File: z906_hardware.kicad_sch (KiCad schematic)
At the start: 22 parts, among them J1 USB_C_Receptacle_USB2.0_14P, J3 DE_15 Amplifier, J4 DE15 Console, U1 ESP32-S3-WROOM-1, U2 AP63203WU, U3 PCM5102A, U4 TPD2EUSB30, U5 TPD1E05U06DYA, U6 TPS7A4533

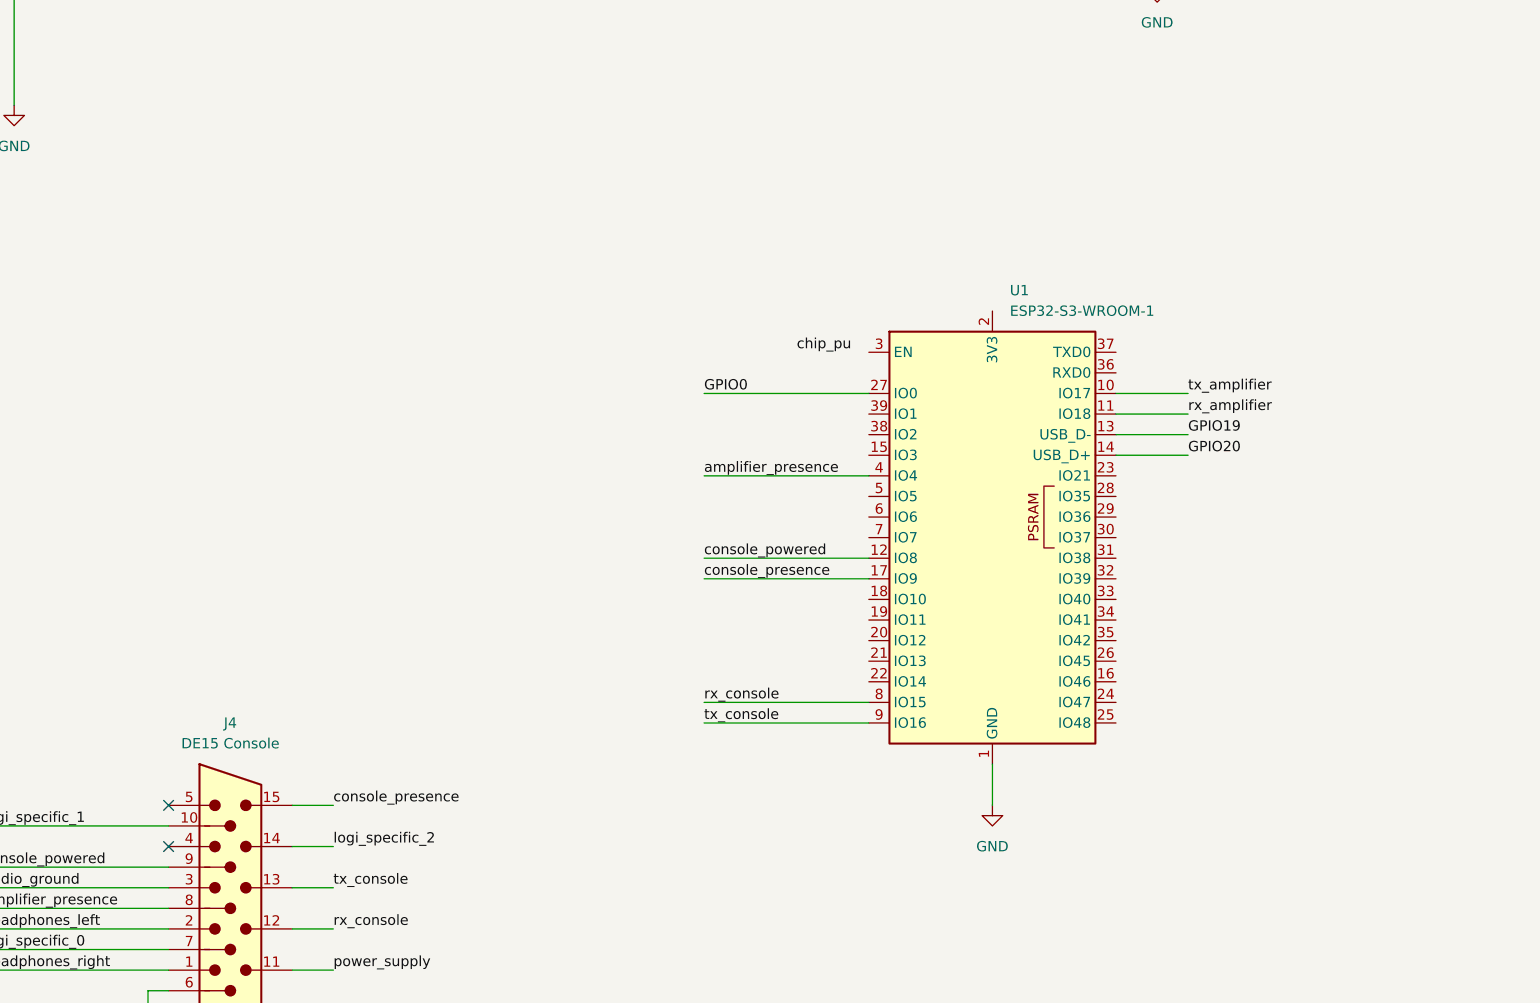
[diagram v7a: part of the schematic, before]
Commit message: add pcm1860
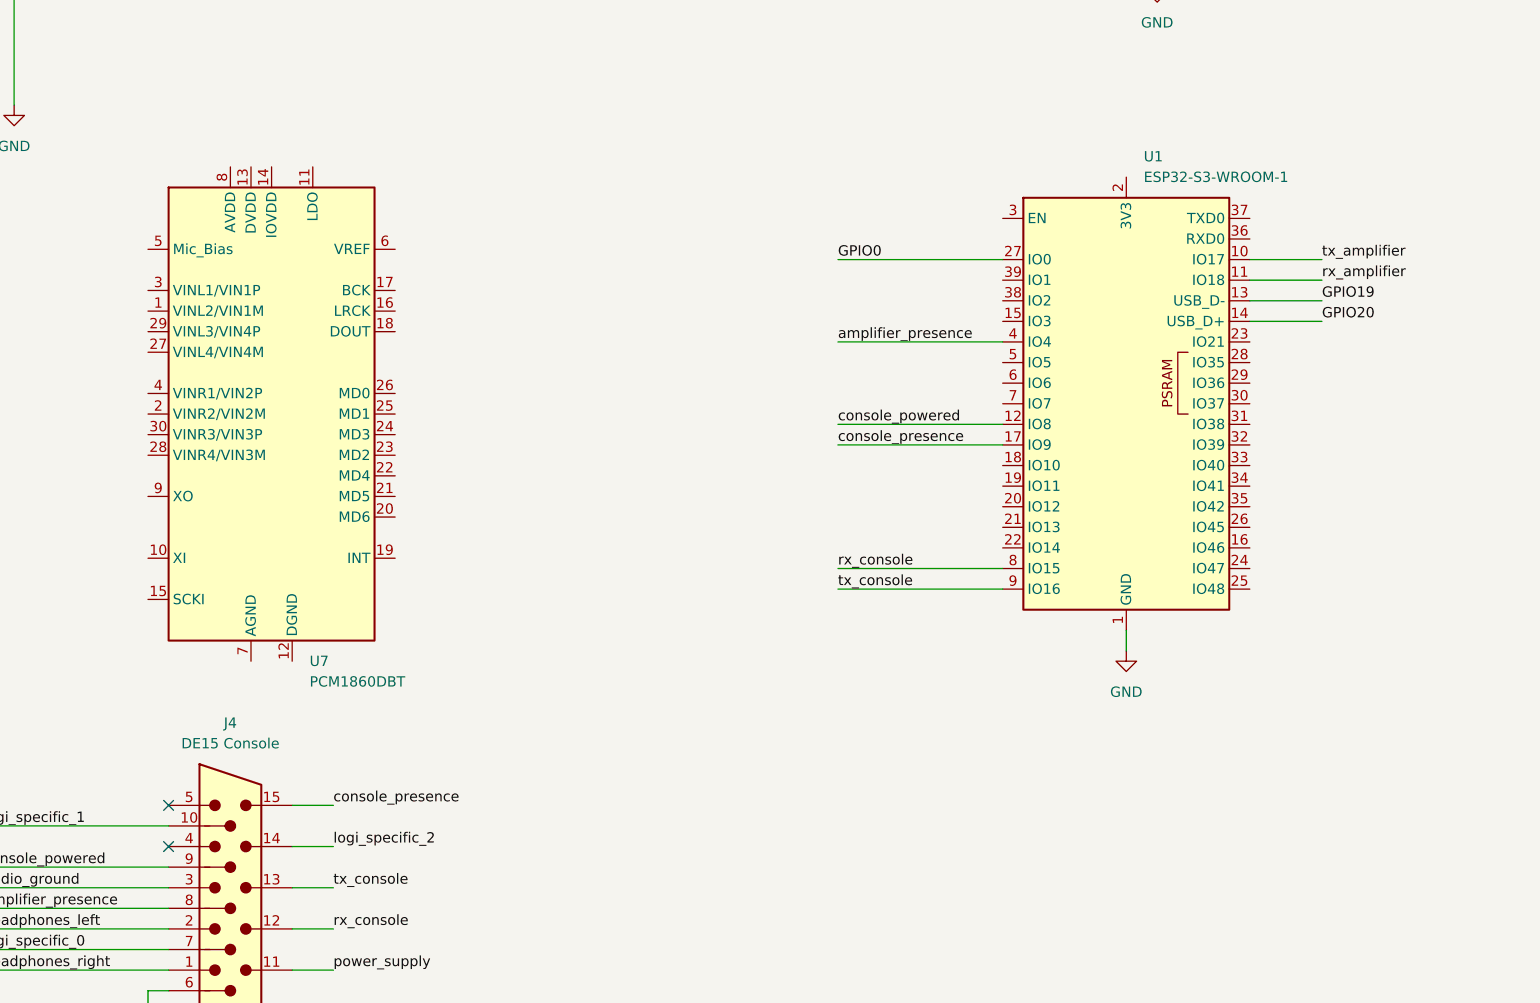
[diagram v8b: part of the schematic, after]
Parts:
- added U7: PCM1860DBT, Package_SO:TSSOP-30_4.4x7.8mm_P0.5mm, symbol Audio:PCM1860DBT
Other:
- moved on the sheet: U1
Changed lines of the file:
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@@
 	(wire
 		(pts
-			(xy 182.88 146.05) (xy 203.2 146.05)
+			(xy 199.39 129.54) (xy 219.71 129.54)
 		)
 		(stroke
@@
 	(wire
 		(pts
-			(xy 182.88 115.57) (xy 203.2 115.57)
+			(xy 199.39 99.06) (xy 219.71 99.06)
 		)
 		(stroke
@@
 	(wire
 		(pts
-			(xy 233.68 107.95) (xy 242.57 107.95)
+			(xy 250.19 91.44) (xy 259.08 91.44)
 		)
 		(stroke
@@
 	(wire
 		(pts
-			(xy 182.88 128.27) (xy 203.2 128.27)
+			(xy 199.39 111.76) (xy 219.71 111.76)
 		)
 		(stroke
@@
 	(wire
 		(pts
-			(xy 182.88 105.41) (xy 203.2 105.41)
+			(xy 199.39 88.9) (xy 219.71 88.9)
 		)
 		(stroke
@@
 	(wire
 		(pts
-			(xy 218.44 151.13) (xy 218.44 156.21)
+			(xy 234.95 134.62) (xy 234.95 137.16)
 		)
 		(stroke
@@
 	(wire
 		(pts
-			(xy 233.68 113.03) (xy 242.57 113.03)
+			(xy 250.19 96.52) (xy 259.08 96.52)
 		)
 		(stroke
@@
 	(wire
 		(pts
-			(xy 233.68 110.49) (xy 242.57 110.49)
+			(xy 250.19 93.98) (xy 259.08 93.98)
 		)
 		(stroke
@@
 	(wire
 		(pts
-			(xy 182.88 125.73) (xy 203.2 125.73)
+			(xy 199.39 109.22) (xy 219.71 109.22)
 		)
 		(stroke
@@
 	(wire
 		(pts
-			(xy 233.68 105.41) (xy 242.57 105.41)
+			(xy 250.19 88.9) (xy 259.08 88.9)
 		)
 		(stroke
@@
 	(wire
 		(pts
-			(xy 182.88 143.51) (xy 203.2 143.51)
+			(xy 199.39 127) (xy 219.71 127)
 		)
 		(stroke
@@
 	)
 	(label "rx_amplifier"
-		(at 242.57 107.95 0)
+		(at 259.08 91.44 0)
 		(effects
 			(font
@@
 	)
 	(label "tx_console"
-		(at 182.88 146.05 0)
+		(at 199.39 129.54 0)
 		(effects
 			(font
@@
 	)
 	(label "GPIO0"
-		(at 182.88 105.41 0)
+		(at 199.39 88.9 0)
 		(effects
 			(font
@@
 	)
 	(label "GPIO19"
-		(at 242.57 110.49 0)
+		(at 259.08 93.98 0)
 		(effects
 			(font
@@
 	)
 	(label "console_powered"
-		(at 182.88 125.73 0)
+		(at 199.39 109.22 0)
 		(effects
 			(font
@@
 		)
 	)
-	(label "chip_pu"
-		(at 194.31 100.33 0)
-		(effects
-			(font
-				(size 1.27 1.27)
-			)
-			(justify left bottom)
-		)
-	)
 	(label "rx_console"
-		(at 182.88 143.51 0)
+		(at 199.39 127 0)
 		(effects
 			(font
@@
 	)
 	(label "tx_amplifier"
-		(at 242.57 105.41 0)
+		(at 259.08 88.9 0)
 		(effects
 			(font
@@
 	)
 	(label "amplifier_presence"
-		(at 182.88 115.57 0)
+		(at 199.39 99.06 0)
 		(effects
 			(font
@@
 	)
 	(label "GPIO20"
-		(at 242.57 113.03 0)
+		(at 259.08 96.52 0)
 		(effects
 			(font
@@
 	)
 	(label "console_presence"
-		(at 182.88 128.27 0)
+		(at 199.39 111.76 0)
 		(effects
 			(font
@@
 	)
 	(symbol
+		(lib_id "Audio:PCM1860DBT")
+		(at 129.54 107.95 0)
+		(unit 1)
+		(body_style 1)
+		(exclude_from_sim no)
+		(in_bom yes)
+		(on_board yes)
+		(in_pos_files yes)
+		(dnp no)
+		(fields_autoplaced yes)
+		(property "Reference" "U7"
+			(at 134.2233 138.43 0)
+			(show_name no)
+			(do_not_autoplace no)
+			(effects
+				(font
+					(size 1.27 1.27)
+				)
+				(justify left)
+			)
+		)
+		(property "Value" "PCM1860DBT"
+			(at 134.2233 140.97 0)
+			(show_name no)
+			(do_not_autoplace no)
+			(effects
+				(font
+					(size 1.27 1.27)
+				)
+				(justify left)
+			)
+		)
+		(property "Footprint" "Package_SO:TSSOP-30_4.4x7.8mm_P0.5mm"
+			(at 134.874 139.954 0)
+			(hide yes)
+			(show_name no)
+			(do_not_autoplace no)
+			(effects
+				(font
+					(size 1.27 1.27)
+				)
+				(justify left)
+			)
+		)
+		(property "Datasheet" "https://www.ti.com/lit/ds/symlink/pcm1860.pdf"
+			(at 134.874 142.24 0)
+			(hide yes)
+			(show_name no)
+			(do_not_autoplace no)
+			(effects
+				(font
+					(size 1.27 1.27)
+				)
+				(justify left)
+			)
+		)
+		(property "Description" "2-Channel, 192 kHz, 24-bit, Audio ADC, 103dB SNR, I2S / left-justified digital output formats, hardware control interface, TSSOP-30"
+			(at 129.54 107.95 0)
+			(hide yes)
+			(show_name no)
+			(do_not_autoplace no)
+			(effects
+				(font
+					(size 1.27 1.27)
+				)
+			)
+		)
+		(pin "12"
+		)
+		(pin "26"
+		)
+		(pin "30"
+		)
+		(pin "3"
+		)
+		(pin "5"
+		)
+		(pin "28"
+		)
+		(pin "1"
+		)
+		(pin "4"
+		)
+		(pin "6"
+		)
+		(pin "25"
+		)
+		(pin "29"
+		)
+		(pin "8"
+		)
+		(pin "9"
+		)
+		(pin "11"
+		)
+		(pin "15"
+		)
+		(pin "27"
+		)
+		(pin "19"
+		)
+		(pin "13"
+		)
+		(pin "7"
+		)
+		(pin "2"
+		)
+		(pin "10"
+		)
+		(pin "18"
+		)
+		(pin "16"
+		)
+		(pin "23"
+		)
+		(pin "20"
+		)
+		(pin "24"
+		)
+		(pin "17"
+		)
+		(pin "14"
+		)
+		(pin "22"
+		)
+		(pin "21"
+		)
+		(instances
+			(project "z906_hardware"
+				(path "/eb724320-f684-4550-84c5-ad44b13c3624"
+					(reference "U7")
+					(unit 1)
+				)
+			)
+		)
+	)
+	(symbol
 		(lib_id "Device:R")
 		(at 54.61 53.34 0)
@@
 	(symbol
 		(lib_id "RF_Module:ESP32-S3-WROOM-1")
-		(at 218.44 123.19 0)
+		(at 234.95 106.68 0)
 		(unit 1)
 		(body_style 1)
@@
 		(fields_autoplaced yes)
 		(property "Reference" "U1"
-			(at 220.5833 92.71 0)
+			(at 237.0933 76.2 0)
 			(show_name no)
 			(do_not_autoplace no)
@@
 		)
 		(property "Value" "ESP32-S3-WROOM-1"
-			(at 220.5833 95.25 0)
+			(at 237.0933 78.74 0)
 			(show_name no)
 			(do_not_autoplace no)
@@
 		)
 		(property "Footprint" "RF_Module:ESP32-S3-WROOM-1"
-			(at 218.44 120.65 0)
+			(at 234.95 104.14 0)
 			(hide yes)
 			(show_name no)
@@
 		)
 		(property "Datasheet" "https://www.espressif.com/sites/default/files/documentation/esp32-s3-wroom-1_wroom-1u_datasheet_en.pdf"
-			(at 218.44 123.19 0)
+			(at 234.95 106.68 0)
 			(hide yes)
 			(show_name no)
@@
 		)
 		(property "Description" "RF Module, ESP32-S3 SoC, Wi-Fi 802.11b/g/n, Bluetooth, BLE, 32-bit, 3.3V, onboard antenna, SMD"
-			(at 218.44 123.19 0)
+			(at 234.95 106.68 0)
 			(hide yes)
 			(show_name no)
@@
 	(symbol
 		(lib_id "power:GND")
-		(at 218.44 156.21 0)
+		(at 234.95 137.16 0)
 		(unit 1)
 		(body_style 1)
@@
 		(fields_autoplaced yes)
 		(property "Reference" "#PWR05"
-			(at 218.44 162.56 0)
+			(at 234.95 143.51 0)
 			(hide yes)
 			(show_name no)
@@
 		)
 		(property "Value" "GND"
-			(at 218.44 161.29 0)
+			(at 234.95 142.24 0)
 			(show_name no)
 			(do_not_autoplace no)
@@
 		)
 		(property "Footprint" ""
-			(at 218.44 156.21 0)
+			(at 234.95 137.16 0)
 			(hide yes)
 			(show_name no)
@@
 		)
 		(property "Datasheet" ""
-			(at 218.44 156.21 0)
+			(at 234.95 137.16 0)
 			(hide yes)
 			(show_name no)
@@
 		)
 		(property "Description" "Power symbol creates a global label with name \"GND\" , ground"
-			(at 218.44 156.21 0)
+			(at 234.95 137.16 0)
 			(hide yes)
 			(show_name no)
